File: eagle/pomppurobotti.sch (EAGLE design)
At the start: 3 parts

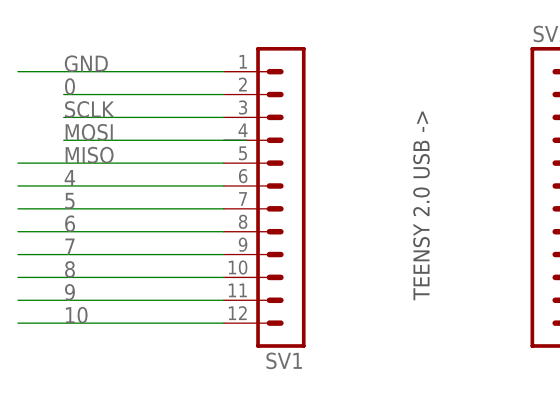
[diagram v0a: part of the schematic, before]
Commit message: Updates to schemantic and board files
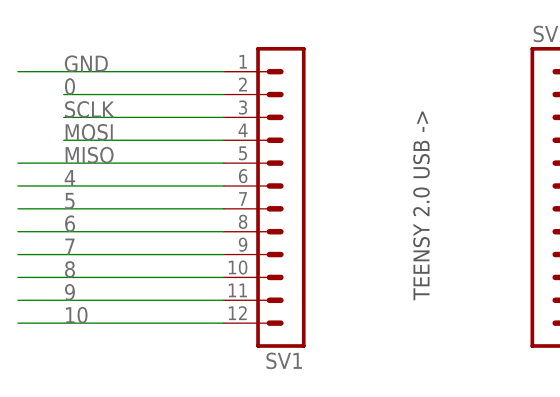
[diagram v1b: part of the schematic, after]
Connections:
- net MOSI: now also SV1.4
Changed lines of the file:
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@@
 <net name="MOSI" class="0">
 <segment>
-<wire x1="55.88" y1="45.72" x2="35.56" y2="45.72" width="0.1524" layer="91"/>
+<wire x1="53.34" y1="45.72" x2="35.56" y2="45.72" width="0.1524" layer="91"/>
 <label x="35.56" y="45.72" size="1.778" layer="95"/>
+<pinref part="SV1" gate="1" pin="4"/>
 </segment>
 <segment>

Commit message: First version of PCB
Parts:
- removed SV1, SV2: (no value), con-lstb:MA12-1
- removed SV3: (no value), con-lstb:MA08-1
- added ACCELOM: (no value), SparkFun-Connectors:M06SILK_FEMALE_PTH
- added C1, C2: 10uF, SparkFun-Capacitors:CAPPTH
- added EXTRA: (no value), SparkFun-Connectors:M03PTH
- added IC1: (no value), SparkFun-PowerIC:V_REG_78XX-TO-220
- added JP1: POWER_JACK1, SparkFun-Connectors:POWER_JACK1
- added LED1, LED2: RED, SparkFun-LED:LED5MM
- added MORORD_R, MOTORD_L: (no value), SparkFun-Connectors:M08LONGPADS
- added MOTORS: (no value), SparkFun-Connectors:M04PTH
- added PIEZO: EFBAA40D101, buzzer:EFBAA40D101
- added Q1: MOSFET-NCHANNELFQP30N06L, SparkFun-DiscreteSemi:MOSFET-NCHANNELFQP30N06L
- added R1, R2: 220Ω, SparkFun-Resistors:RESISTORAXIAL-0.3
- added RADIO: (no value), SparkFun-Connectors:M08
- added RANGEF: (no value), SparkFun-Connectors:M05PTH
- added RV1: (no value), SparkFun-Electromechanical:POTTRIM
- added S1: SWITCH-MOMENTARY-2PTH, SparkFun-Electromechanical:SWITCH-MOMENTARY-2PTH
- added SPRING_PINS: M02PTH, SparkFun-Connectors:M02PTH
- added TEENSY_1, TEENSY_2: M12PTH, SparkFun-Connectors:M12PTH
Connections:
- removed net +5V: SV2.12, SV3.1
- removed net 0: SV1.2
- removed net 10: SV1.12
- removed net 4: SV1.6
- removed net 5: SV1.7
- removed net 6: SV1.8
- removed net 7: SV1.9
- removed net 8: SV1.10
- removed net 9: SV1.11
- removed net N$14: SV2.11
- removed net N$15: SV2.10
- removed net N$16: SV2.9
- removed net N$17: SV2.8
- removed net N$18: SV2.7
- removed net N$19: SV2.6
- removed net N$20: SV2.5
- removed net N$21: SV2.4
- removed net N$22: SV2.3
- removed net N$23: SV2.2
- removed net N$24: SV2.1
- new net A0: ACCELOM.2, TEENSY_2.9
- new net A01: MOTORD_L.4, MOTORS.4
- new net A02: MOTORD_L.5, MOTORS.3
- new net A1: ACCELOM.3, TEENSY_2.10
- new net A2: ACCELOM.4, TEENSY_2.11
- new net A4: EXTRA.1, TEENSY_2.7
- new net A5: EXTRA.2, TEENSY_2.6
- new net A8: RV1.S, TEENSY_2.3
- new net AIN1: MORORD_R.6, TEENSY_1.8
- new net AIN2: MORORD_R.7, TEENSY_1.2
- new net AN: RANGEF.1, TEENSY_2.8
- new net B01: MOTORD_L.7, MOTORS.1
- new net B02: MOTORD_L.6, MOTORS.2
- new net BIN1: MORORD_R.4, TEENSY_1.9
- new net BIN2: MORORD_R.3, TEENSY_1.10
- new net LEDA10: R2.1, TEENSY_2.1
- new net N$2: LED1.C, R1.2
- new net N$3: C1.1, IC1.IN, JP1.PWR
- new net N$4: LED2.A, R2.2
- new net N$5: Q1.D, SPRING_PINS.2
- new net PWMA: MORORD_R.8, TEENSY_1.12, TEENSY_1.6
- new net PWMA6: EXTRA.3, TEENSY_2.5
- new net PWMA7: PIEZO.2, TEENSY_2.4
- new net PWMA9: S1.1, TEENSY_2.2
- new net PWMB: MORORD_R.2, TEENSY_1.11
- new net PWMC: Q1.G, TEENSY_1.7
- new net VCC: ACCELOM.6, C2.1, IC1.OUT, LED1.A, MORORD_R.5, MOTORD_L.1, MOTORD_L.2, Q1.S, RADIO.1, RANGEF.4, RV1.A, S1.2, TEENSY_2.12
- net +3.3V: now also RADIO.8; no longer SV3.8
- net GND: now also ACCELOM.5, C1.2, C2.2, IC1.GND, JP1.GND, LED2.C, MORORD_R.1, MOTORD_L.3, MOTORD_L.8, PIEZO.1, R1.1, RADIO.2, RANGEF.5, RV1.E, SPRING_PINS.1, TEENSY_1.1; no longer SV1.1, SV3.2
- net IRQ: now also RADIO.7; no longer SV3.7
- net MISO: now also RADIO.4, TEENSY_1.5; no longer SV1.5, SV3.4
- net MOSI: now also RADIO.5, TEENSY_1.4; no longer SV1.4, SV3.5
- net SCLK: now also RADIO.3, TEENSY_1.3; no longer SV1.3, SV3.3
- net SEL: now also RADIO.6; no longer SV3.6
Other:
- note added: "ACCELOMETER ADXL335"
- note added: "EXTRA PINS"
- note added: "PIEZO ELEMENT PKM17EPP-4001-B0"
- note added: "POWER SOURCE, 5V VOLTAGE REGULATOR"
- note added: "RADIO (CHECK TYPE!)"
- note added: "RANGE FINDER MAXSONAR-EZ1"
- note added: "SPARKFUN MOTOR DRIVER TB6612FNG"
- note removed: "RADIO"

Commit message: Many major improvements
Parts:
- added POWER_INPUT_2: M02PTH, SparkFun-Connectors:M02PTH
- JP1: value POWER_JACK1 -> POWER_JACKPTH; device SparkFun-Connectors:POWER_JACK1 -> SparkFun-Connectors:POWER_JACKPTH
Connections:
- net GND: now also POWER_INPUT_2.1
- net N$3: now also POWER_INPUT_2.2
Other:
- note added: "POWER SOURCE (JACK OR HEADER), 5V VOLTAGE REGULATOR"
- note added: "RANGE FINDER MAXSONAR-EZ1 (5 OF 7 PINS)"
- note removed: "POWER SOURCE, 5V VOLTAGE REGULATOR"
- note removed: "RANGE FINDER MAXSONAR-EZ1"
- moved on the sheet: JP1
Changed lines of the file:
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@@
 <grid distance="0.1" unitdist="inch" unit="inch" style="lines" multiple="1" display="no" altdistance="0.01" altunitdist="inch" altunit="inch"/>
 <layers>
-<layer number="1" name="Top" color="4" fill="1" visible="no" active="no"/>
-<layer number="16" name="Bottom" color="1" fill="1" visible="no" active="no"/>
-<layer number="17" name="Pads" color="2" fill="1" visible="no" active="no"/>
-<layer number="18" name="Vias" color="2" fill="1" visible="no" active="no"/>
-<layer number="19" name="Unrouted" color="6" fill="1" visible="no" active="no"/>
-<layer number="20" name="Dimension" color="15" fill="1" visible="no" active="no"/>
-<layer number="21" name="tPlace" color="7" fill="1" visible="no" active="no"/>
-<layer number="22" name="bPlace" color="7" fill="1" visible="no" active="no"/>
-<layer number="23" name="tOrigins" color="15" fill="1" visible="no" active="no"/>
-<layer number="24" name="bOrigins" color="15" fill="1" visible="no" active="no"/>
-<layer number="25" name="tNames" color="7" fill="1" visible="no" active="no"/>
-<layer number="26" name="bNames" color="7" fill="1" visible="no" active="no"/>
-<layer number="27" name="tValues" color="7" fill="1" visible="no" active="no"/>
-<layer number="28" name="bValues" color="7" fill="1" visible="no" active="no"/>
+<layer number="1" name="Top" color="4" fill="1" visible="yes" active="no"/>
+<layer number="16" name="Bottom" color="1" fill="1" visible="yes" active="no"/>
+<layer number="17" name="Pads" color="2" fill="1" visible="yes" active="no"/>
+<layer number="18" name="Vias" color="2" fill="1" visible="yes" active="no"/>
+<layer number="19" name="Unrouted" color="6" fill="1" visible="yes" active="no"/>
+<layer number="20" name="Dimension" color="15" fill="1" visible="yes" active="no"/>
+<layer number="21" name="tPlace" color="16" fill="1" visible="yes" active="no"/>
+<layer number="22" name="bPlace" color="14" fill="1" visible="yes" active="no"/>
+<layer number="23" name="tOrigins" color="15" fill="1" visible="yes" active="no"/>
+<layer number="24" name="bOrigins" color="15" fill="1" visible="yes" active="no"/>
+<layer number="25" name="tNames" color="7" fill="1" visible="yes" active="no"/>
+<layer number="26" name="bNames" color="7" fill="1" visible="yes" active="no"/>
+<layer number="27" name="tValues" color="7" fill="1" visible="yes" active="no"/>
+<layer number="28" name="bValues" color="7" fill="1" visible="yes" active="no"/>
 <layer number="29" name="tStop" color="7" fill="3" visible="no" active="no"/>
 <layer number="30" name="bStop" color="7" fill="6" visible="no" active="no"/>
@@
 <layer number="35" name="tGlue" color="7" fill="4" visible="no" active="no"/>
 <layer number="36" name="bGlue" color="7" fill="5" visible="no" active="no"/>
-<layer number="37" name="tTest" color="7" fill="1" visible="no" active="no"/>
-<layer number="38" name="bTest" color="7" fill="1" visible="no" active="no"/>
+<layer number="37" name="tTest" color="7" fill="1" visible="yes" active="no"/>
+<layer number="38" name="bTest" color="7" fill="1" visible="yes" active="no"/>
 <layer number="39" name="tKeepout" color="4" fill="11" visible="no" active="no"/>
 <layer number="40" name="bKeepout" color="1" fill="11" visible="no" active="no"/>
@@
 <layer number="44" name="Drills" color="7" fill="1" visible="no" active="no"/>
 <layer number="45" name="Holes" color="7" fill="1" visible="no" active="no"/>
-<layer number="46" name="Milling" color="3" fill="1" visible="no" active="no"/>
-<layer number="47" name="Measures" color="7" fill="1" visible="no" active="no"/>
-<layer number="48" name="Document" color="7" fill="1" visible="no" active="no"/>
-<layer number="49" name="Reference" color="7" fill="1" visible="no" active="no"/>
-<layer number="50" name="dxf" color="7" fill="1" visible="no" active="no"/>
-<layer number="51" name="tDocu" color="7" fill="1" visible="no" active="no"/>
-<layer number="52" name="bDocu" color="7" fill="1" visible="no" active="no"/>
-<layer number="53" name="tGND_GNDA" color="7" fill="9" visible="no" active="no"/>
-<layer number="54" name="bGND_GNDA" color="1" fill="9" visible="no" active="no"/>
-<layer number="56" name="wert" color="7" fill="1" visible="no" active="no"/>
-<layer number="57" name="tCAD" color="7" fill="1" visible="no" active="no"/>
+<layer number="46" name="Milling" color="3" fill="1" visible="yes" active="no"/>
+<layer number="47" name="Measures" color="7" fill="1" visible="yes" active="no"/>
+<layer number="48" name="Document" color="7" fill="1" visible="yes" active="no"/>
+<layer number="49" name="Reference" color="7" fill="1" visible="yes" active="no"/>
+<layer number="50" name="dxf" color="7" fill="1" visible="yes" active="no"/>
+<layer number="51" name="tDocu" color="6" fill="1" visible="yes" active="no"/>
+<layer number="52" name="bDocu" color="7" fill="1" visible="yes" active="no"/>
+<layer number="53" name="tGND_GNDA" color="7" fill="9" visible="yes" active="no"/>
+<layer number="54" name="bGND_GNDA" color="1" fill="9" visible="yes" active="no"/>
+<layer number="56" name="wert" color="7" fill="1" visible="yes" active="no"/>
+<layer number="57" name="tCAD" color="7" fill="1" visible="yes" active="no"/>
 <layer number="90" name="Modules" color="5" fill="1" visible="yes" active="yes"/>
 <layer number="91" name="Nets" color="13" fill="1" visible="yes" active="yes"/>
@@
 </part>
 <part name="IC1" library="SparkFun-PowerIC" deviceset="V_REG_78XX" device="-TO-220"/>
-<part name="JP1" library="SparkFun-Connectors" deviceset="POWER_JACK" device="1"/>
+<part name="JP1" library="SparkFun-Connectors" deviceset="POWER_JACK" device="PTH" value="POWER_JACKPTH"/>
 <part name="GND1" library="SparkFun-Aesthetics" deviceset="GND" device=""/>
 <part name="SUPPLY3" library="SparkFun-Aesthetics" deviceset="VCC" device=""/>
@@
 <part name="GND8" library="SparkFun-Aesthetics" deviceset="GND" device=""/>
 <part name="RV1" library="SparkFun-Electromechanical" deviceset="POT" device="TRIM"/>
+<part name="POWER_INPUT_2" library="SparkFun-Connectors" deviceset="M02" device="PTH"/>
 </parts>
 <sheets>
@@
 <text x="160.02" y="53.34" size="1.778" layer="91">ACCELOMETER
 ADXL335</text>
-<text x="93.98" y="63.5" size="1.778" layer="91">POWER SOURCE,
+<text x="93.98" y="63.5" size="1.778" layer="91">POWER SOURCE (JACK OR HEADER),
 5V VOLTAGE REGULATOR </text>
 <text x="220.98" y="-15.24" size="1.778" layer="91">PIEZO ELEMENT
 PKM17EPP-4001-B0</text>
 <text x="200.66" y="53.34" size="1.778" layer="91">RANGE FINDER
-MAXSONAR-EZ1</text>
+MAXSONAR-EZ1
+(5 OF 7 PINS)</text>
 <text x="238.76" y="5.08" size="1.778" layer="91">EXTRA
 PINS</text>
+<circle x="127" y="-5.08" radius="5.6796125" width="0.1524" layer="91"/>
+<circle x="121.92" y="54.61" radius="7.184203125" width="0.1524" layer="91"/>
 </plain>
 <instances>
@@
 </instance>
 <instance part="IC1" gate="G$1" x="121.92" y="55.88"/>
-<instance part="JP1" gate="G$1" x="104.14" y="48.26"/>
+<instance part="JP1" gate="G$1" x="88.9" y="48.26"/>
 <instance part="GND1" gate="1" x="121.92" y="35.56"/>
 <instance part="SUPPLY3" gate="G$1" x="182.88" y="-53.34" rot="R270"/>
@@
 <instance part="GND8" gate="1" x="203.2" y="-38.1" rot="R270"/>
 <instance part="RV1" gate="G$1" x="213.36" y="-38.1" rot="R90"/>
+<instance part="POWER_INPUT_2" gate="G$1" x="96.52" y="48.26"/>
 </instances>
 <busses>
@@
 <pinref part="JP1" gate="G$1" pin="GND"/>
 <wire x1="121.92" y1="43.18" x2="111.76" y2="43.18" width="0.1524" layer="91"/>
-<wire x1="111.76" y1="43.18" x2="106.68" y2="43.18" width="0.1524" layer="91"/>
-<wire x1="106.68" y1="43.18" x2="106.68" y2="50.8" width="0.1524" layer="91"/>
+<wire x1="111.76" y1="43.18" x2="104.14" y2="43.18" width="0.1524" layer="91"/>
+<wire x1="104.14" y1="43.18" x2="91.44" y2="43.18" width="0.1524" layer="91"/>
+<wire x1="91.44" y1="43.18" x2="91.44" y2="50.8" width="0.1524" layer="91"/>
 <wire x1="121.92" y1="43.18" x2="121.92" y2="38.1" width="0.1524" layer="91"/>
 <junction x="121.92" y="43.18"/>
@@
 <wire x1="132.08" y1="43.18" x2="134.62" y2="43.18" width="0.1524" layer="91"/>
 <junction x="132.08" y="43.18"/>
+<pinref part="POWER_INPUT_2" gate="G$1" pin="1"/>
+<wire x1="104.14" y1="48.26" x2="104.14" y2="43.18" width="0.1524" layer="91"/>
+<junction x="104.14" y="43.18"/>
 </segment>
 <segment>
@@
 <pinref part="JP1" gate="G$1" pin="PWR"/>
 <pinref part="IC1" gate="G$1" pin="IN"/>
-<wire x1="106.68" y1="55.88" x2="111.76" y2="55.88" width="0.1524" layer="91"/>
+<wire x1="91.44" y1="55.88" x2="104.14" y2="55.88" width="0.1524" layer="91"/>
+<wire x1="104.14" y1="55.88" x2="111.76" y2="55.88" width="0.1524" layer="91"/>
 <wire x1="111.76" y1="55.88" x2="114.3" y2="55.88" width="0.1524" layer="91"/>
 <wire x1="111.76" y1="53.34" x2="111.76" y2="55.88" width="0.1524" layer="91"/>
 <junction x="111.76" y="55.88"/>
 <pinref part="C1" gate="G$1" pin="1"/>
-</segment>
-</net>
+<pinref part="POWER_INPUT_2" gate="G$1" pin="2"/>
+<wire x1="104.14" y1="50.8" x2="104.14" y2="55.88" width="0.1524" layer="91"/>
+<junction x="104.14" y="55.88"/>
+</segment>
+</net>

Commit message: Fix to proximity sensor position etc
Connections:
- new net PWMD: TEENSY_1.12
- net PWMA: no longer TEENSY_1.12
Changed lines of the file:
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@@
 <grid distance="0.1" unitdist="inch" unit="inch" style="lines" multiple="1" display="no" altdistance="0.01" altunitdist="inch" altunit="inch"/>
 <layers>
-<layer number="1" name="Top" color="4" fill="1" visible="yes" active="no"/>
-<layer number="16" name="Bottom" color="1" fill="1" visible="yes" active="no"/>
-<layer number="17" name="Pads" color="2" fill="1" visible="yes" active="no"/>
-<layer number="18" name="Vias" color="2" fill="1" visible="yes" active="no"/>
-<layer number="19" name="Unrouted" color="6" fill="1" visible="yes" active="no"/>
-<layer number="20" name="Dimension" color="15" fill="1" visible="yes" active="no"/>
-<layer number="21" name="tPlace" color="16" fill="1" visible="yes" active="no"/>
-<layer number="22" name="bPlace" color="14" fill="1" visible="yes" active="no"/>
-<layer number="23" name="tOrigins" color="15" fill="1" visible="yes" active="no"/>
-<layer number="24" name="bOrigins" color="15" fill="1" visible="yes" active="no"/>
-<layer number="25" name="tNames" color="7" fill="1" visible="yes" active="no"/>
-<layer number="26" name="bNames" color="7" fill="1" visible="yes" active="no"/>
-<layer number="27" name="tValues" color="7" fill="1" visible="yes" active="no"/>
-<layer number="28" name="bValues" color="7" fill="1" visible="yes" active="no"/>
+<layer number="1" name="Top" color="4" fill="1" visible="no" active="no"/>
+<layer number="16" name="Bottom" color="1" fill="1" visible="no" active="no"/>
+<layer number="17" name="Pads" color="2" fill="1" visible="no" active="no"/>
+<layer number="18" name="Vias" color="2" fill="1" visible="no" active="no"/>
+<layer number="19" name="Unrouted" color="6" fill="1" visible="no" active="no"/>
+<layer number="20" name="Dimension" color="15" fill="1" visible="no" active="no"/>
+<layer number="21" name="tPlace" color="16" fill="1" visible="no" active="no"/>
+<layer number="22" name="bPlace" color="14" fill="1" visible="no" active="no"/>
+<layer number="23" name="tOrigins" color="15" fill="1" visible="no" active="no"/>
+<layer number="24" name="bOrigins" color="15" fill="1" visible="no" active="no"/>
+<layer number="25" name="tNames" color="7" fill="1" visible="no" active="no"/>
+<layer number="26" name="bNames" color="7" fill="1" visible="no" active="no"/>
+<layer number="27" name="tValues" color="7" fill="1" visible="no" active="no"/>
+<layer number="28" name="bValues" color="7" fill="1" visible="no" active="no"/>
 <layer number="29" name="tStop" color="7" fill="3" visible="no" active="no"/>
 <layer number="30" name="bStop" color="7" fill="6" visible="no" active="no"/>
@@
 <layer number="35" name="tGlue" color="7" fill="4" visible="no" active="no"/>
 <layer number="36" name="bGlue" color="7" fill="5" visible="no" active="no"/>
-<layer number="37" name="tTest" color="7" fill="1" visible="yes" active="no"/>
-<layer number="38" name="bTest" color="7" fill="1" visible="yes" active="no"/>
+<layer number="37" name="tTest" color="7" fill="1" visible="no" active="no"/>
+<layer number="38" name="bTest" color="7" fill="1" visible="no" active="no"/>
 <layer number="39" name="tKeepout" color="4" fill="11" visible="no" active="no"/>
 <layer number="40" name="bKeepout" color="1" fill="11" visible="no" active="no"/>
@@
 <layer number="44" name="Drills" color="7" fill="1" visible="no" active="no"/>
 <layer number="45" name="Holes" color="7" fill="1" visible="no" active="no"/>
-<layer number="46" name="Milling" color="3" fill="1" visible="yes" active="no"/>
-<layer number="47" name="Measures" color="7" fill="1" visible="yes" active="no"/>
-<layer number="48" name="Document" color="7" fill="1" visible="yes" active="no"/>
-<layer number="49" name="Reference" color="7" fill="1" visible="yes" active="no"/>
-<layer number="50" name="dxf" color="7" fill="1" visible="yes" active="no"/>
-<layer number="51" name="tDocu" color="6" fill="1" visible="yes" active="no"/>
-<layer number="52" name="bDocu" color="7" fill="1" visible="yes" active="no"/>
-<layer number="53" name="tGND_GNDA" color="7" fill="9" visible="yes" active="no"/>
-<layer number="54" name="bGND_GNDA" color="1" fill="9" visible="yes" active="no"/>
-<layer number="56" name="wert" color="7" fill="1" visible="yes" active="no"/>
-<layer number="57" name="tCAD" color="7" fill="1" visible="yes" active="no"/>
+<layer number="46" name="Milling" color="3" fill="1" visible="no" active="no"/>
+<layer number="47" name="Measures" color="7" fill="1" visible="no" active="no"/>
+<layer number="48" name="Document" color="7" fill="1" visible="no" active="no"/>
+<layer number="49" name="Reference" color="7" fill="1" visible="no" active="no"/>
+<layer number="50" name="dxf" color="7" fill="1" visible="no" active="no"/>
+<layer number="51" name="tDocu" color="6" fill="1" visible="no" active="no"/>
+<layer number="52" name="bDocu" color="7" fill="1" visible="no" active="no"/>
+<layer number="53" name="tGND_GNDA" color="7" fill="9" visible="no" active="no"/>
+<layer number="54" name="bGND_GNDA" color="1" fill="9" visible="no" active="no"/>
+<layer number="56" name="wert" color="7" fill="1" visible="no" active="no"/>
+<layer number="57" name="tCAD" color="7" fill="1" visible="no" active="no"/>
 <layer number="90" name="Modules" color="5" fill="1" visible="yes" active="yes"/>
 <layer number="91" name="Nets" color="13" fill="1" visible="yes" active="yes"/>
@@
 <label x="144.78" y="10.16" size="1.778" layer="95"/>
 </segment>
-<segment>
-<pinref part="TEENSY_1" gate="G$1" pin="12"/>
-<wire x1="152.4" y1="-5.08" x2="144.78" y2="-5.08" width="0.1524" layer="91"/>
-<label x="144.78" y="-5.08" size="1.778" layer="95"/>
-</segment>
 </net>
 <net name="A01" class="0">
@@
 </segment>
 </net>
+<net name="PWMD" class="0">
+<segment>
+<pinref part="TEENSY_1" gate="G$1" pin="12"/>
+<wire x1="152.4" y1="-5.08" x2="144.78" y2="-5.08" width="0.1524" layer="91"/>
+<label x="144.78" y="-5.08" size="1.778" layer="95"/>
+</segment>
+</net>

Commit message: Update the board to use voltage regulator only for Teensy and sensors
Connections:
- removed net N$3: C1.1, IC1.IN, JP1.PWR, POWER_INPUT_2.2
- new net V_BATT: C1.1, IC1.IN, JP1.PWR, MOTORD_L.1, POWER_INPUT_2.2, Q1.S
- net VCC: no longer MOTORD_L.1, Q1.S
